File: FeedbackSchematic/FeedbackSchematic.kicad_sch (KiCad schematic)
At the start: 3 parts

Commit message: invert pin read and finish schematic
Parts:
- added C1, C3, C4: 10u, symbol Device:C
- added C2: 47u, symbol Device:C
- added D1, D11, D12, D2, D21, D22, D31, D32, D41, D42, D51, D52, D61, D62, D71, D72: 1N5822, Diode_THT:D_DO-201AD_P15.24mm_Horizontal, symbol Diode:1N5822
- added D100: 1N4001, Diode_THT:D_DO-41_SOD81_P10.16mm_Horizontal, symbol Diode:1N4001
- added J1: Screw_Terminal_01x02, symbol Connector:Screw_Terminal_01x02
- added J10, J11: Conn_01x02_Male, symbol Connector:Conn_01x02_Male
- added J2: Screw_Terminal_01x08, symbol Connector:Screw_Terminal_01x08
- added J3, J4, J5: Conn_01x08_Male, symbol Connector:Conn_01x08_Male
- added J6, J7: RJ45, symbol Connector:RJ45
- added J8: Conn_01x04_Male, symbol Connector:Conn_01x04_Male
- added J9: Conn_01x03_Male, symbol Connector:Conn_01x03_Male
- added R100, R11, R21, R31, R41, R51, R61, R71: 22k, symbol Device:R
- added R101, R104: 330, symbol Device:R
- added R102, R103: 2k2, symbol Device:R
- added R105: 120, symbol Device:R
- added R12, R22, R32, R42, R52, R62, R72: 4.7k, symbol Device:R
- added R13, R23, R3, R33, R43, R53, R63, R73: 22, symbol Device:R
- added U2, U3: L7805, symbol Regulator_Linear:L7805
- added U4, U5: 6N137, Package_DIP:DIP-8_W7.62mm, symbol Isolator:6N137
- added U6: TJA1050_Board, symbol Symbols_Marcel:TJA1050_Board
- gave numbers to parts that had none: 1
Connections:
- net A5: now reaches U1.10 (PA5_SCK1)
- net A5: now also R51.2, R52.1
- net A6: now reaches U1.11 (PA6_MISO1)
- net A6: now also R61.2, R62.1
- net A7: now reaches U1.12 (PA7_MOSI1)
- net A7: now also R71.2, R72.1
- net at U1.19 (GND): now also J10.1 (Pin_1)
- net at U1.20 (GND): now also J10.2 (Pin_2)
- net at U1.21 (PB12): now also J9.1 (Pin_1)
- net at U1.22 (PB13_SCK2): now also J9.2 (Pin_2)
- net at U1.23 (PB14_MISO2): now also J9.3 (Pin_3)
- net at U1.25 (PA8): now also R100.2
- net at U1.26 (PA9_TX1): now also J8.1 (Pin_1)
- net at U1.27 (PA10_RX1): now also J8.2 (Pin_2)
- net CAN_Rx: now reaches U1.28 (PA11_USB_D-)
- net CAN_Rx: now also J8.3 (Pin_3), R102.1, U5.6 (VO)
- net CAN_Tx: now reaches U1.29 (PA12_USBD+)
- net CAN_Tx: now also J8.4 (Pin_4), U4.3 (C)
- net at U1.30 (PA15): now also J3.1 (Pin_1)
- net at U1.31 (PB3): now also J3.2 (Pin_2)
- net at U1.32 (PB4): now also J3.3 (Pin_3)
- net at U1.33 (PB5): now also J3.4 (Pin_4)
- net at U1.34 (PB6_SCL1): now also J3.5 (Pin_5)
- net at U1.35 (PB7_SDA1): now also J3.6 (Pin_6)
- net at U1.36 (PB8): now also J3.7 (Pin_7)
- net at U1.37 (PB9): now also J3.8 (Pin_8)
- net 5V: now reaches U1.38 (5V_USB)
- net 5V: now also R1.1, C2.1, J4.1 (Pin_1), J4.2 (Pin_2), J4.3 (Pin_3), J4.4 (Pin_4), J4.5 (Pin_5), J4.6 (Pin_6), J4.7 (Pin_7), J4.8 (Pin_8), R11.1, R21.1, R31.1, R41.1, R51.1, R61.1, R71.1, U2.3 (OUT), U5.7 (EN), U5.8 (VCC)
- net GND: now reaches U1.39 (GND)
- net GND: now also R2.2, C1.2, C2.2, D1.1 (K), D2.2 (A), J1.1 (Pin_1), J2.8 (Pin_8), J5.1 (Pin_1), J5.2 (Pin_2), J5.3 (Pin_3), J5.4 (Pin_4), J5.5 (Pin_5), J5.6 (Pin_6), J5.7 (Pin_7), J5.8 (Pin_8), R3.1, U2.2 (GND), U5.5 (GND)
- net 3V3: now reaches U1.40 (VCC3V3)
- net 3V3: now also R101.1, R102.2
- net A0: now reaches U1.5 (PA0)
- net A0: now also R1.2, R2.1
- net A1: now reaches U1.6 (PA1)
- net A1: now also R11.2, R12.1
- net A2: now reaches U1.7 (PA2_TX2)
- net A2: now also R21.2, R22.1
- net A3: now reaches U1.8 (PA3_RX2)
- net A3: now also R31.2, R32.1
- net A4: now reaches U1.9 (PA4)
- net A4: now also R41.2, R42.1
- new net: R101.2, U4.2 (A)
- new net: C3.2, C4.1, J6.6, J7.6, U3.2 (GND), U4.5 (GND), U6.1 (GND)
- new net: R103.1, U4.6 (VO), U6.2 (RX)
- new net: C3.1, R103.2, R104.2, U3.3 (OUT), U4.7 (EN), U4.8 (VCC), U6.4 (VCC)
- new net: D1.2 (A), D11.2 (A), D12.1 (K), D2.1 (K), D21.2 (A), D22.1 (K), D31.2 (A), D32.1 (K), D41.2 (A), D42.1 (K), D51.2 (A), D52.1 (K), D61.2 (A), D62.1 (K), D71.2 (A), D72.1 (K), R13.2, R23.2, R3.2, R33.2, R43.2, R53.2, R63.2, R73.2
- new net: C4.2, J6.7, J7.7, U3.1 (IN)
- new net: J6.1, J7.1
- new net: J6.2, J7.2
- new net: J6.3, J7.3
- new net: J11.2 (Pin_2), J6.4, J7.4, R105.1, U6.5 (CAN_L), U6.6 (CAN_H)
- new net: J6.5, J7.5
- new net: J6.8, J7.8
- new net: U5.3 (C), U6.3 (TX)
- new net: R104.1, U5.2 (A)
- new net: J11.1 (Pin_1), R105.2
- new net: C1.1, D100.1 (K), U2.1 (IN)
- new net Dcc1: D100.2 (A), J1.2 (Pin_2), R100.1
- new net Track1: D11.1 (K), D12.2 (A), J2.7 (Pin_7), R12.2, R13.1
- new net Track2: D21.1 (K), D22.2 (A), J2.6 (Pin_6), R22.2, R23.1
- new net Track3: D31.1 (K), D32.2 (A), J2.5 (Pin_5), R32.2, R33.1
- new net Track4: D41.1 (K), D42.2 (A), J2.4 (Pin_4), R42.2, R43.1
- new net Track5: D51.1 (K), D52.2 (A), J2.3 (Pin_3), R52.2, R53.1
- new net Track6: D61.1 (K), D62.2 (A), J2.2 (Pin_2), R62.2, R63.1
- new net Track7: D71.1 (K), D72.2 (A), J2.1 (Pin_1), R72.2, R73.1
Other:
- moved on the sheet: R1, R2, U1

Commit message: Updated schematics
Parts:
- added D110, D111, D112, D113, D114, D115, D116, D117, D120, D121, D122, D123, D124, D125, D126, D127: LED, symbol Device:LED
- added R110, R111, R112, R113, R114, R115, R116, R117, R120, R121, R122, R123, R124, R125, R126, R127: 470, symbol Device:R
- added U6, U7: 74HC595, symbol 74xx:74HC595
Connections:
- net 5V: now also U6.16 (VCC), U7.16 (VCC)
- net GND: now also D110.1 (K), D111.1 (K), D112.1 (K), D113.1 (K), D114.1 (K), D115.1 (K), D116.1 (K), D117.1 (K), D120.1 (K), D121.1 (K), D122.1 (K), D123.1 (K), D124.1 (K), D125.1 (K), D126.1 (K), D127.1 (K), U6.13 (~{OE}), U6.8 (GND), U7.13 (~{OE}), U7.8 (GND)
- net LedClk: now reaches U1.13 (PB0)
- net LedClk: now also U6.11 (SRCLK), U7.11 (SRCLK)
- net LedData: now reaches U1.14 (PB1)
- net LedData: now also U6.14 (SER)
- net LedOut: now reaches U1.15 (PB10_SCL2)
- net LedOut: now also U6.12 (RCLK), U7.12 (RCLK)
- net LedReset: now reaches U1.16 (PB11_SDA2)
- net LedReset: now also U6.10 (~{SRCLR}), U7.10 (~{SRCLR})
- new net: R113.1, U6.3 (QD)
- new net: D113.2 (A), R113.2
- new net: R111.1, U6.1 (QB)
- new net: R110.1, U6.15 (QA)
- new net: R112.1, U6.2 (QC)
- new net: R114.1, U6.4 (QE)
- new net: R115.1, U6.5 (QF)
- new net: R116.1, U6.6 (QG)
- new net: R117.1, U6.7 (QH)
- new net: U6.9 (QH'), U7.14 (SER)
- new net: R123.1, U7.3 (QD)
- new net: D123.2 (A), R123.2
- new net: R121.1, U7.1 (QB)
- new net: R120.1, U7.15 (QA)
- new net: R122.1, U7.2 (QC)
- new net: R124.1, U7.4 (QE)
- new net: R125.1, U7.5 (QF)
- new net: R126.1, U7.6 (QG)
- new net: R127.1, U7.7 (QH)
- new net: D110.2 (A), R110.2
- new net: D126.2 (A), R126.2
- new net: D116.2 (A), R116.2
- new net: D114.2 (A), R114.2
- new net: D112.2 (A), R112.2
- new net: D120.2 (A), R120.2
- new net: D124.2 (A), R124.2
- new net: D111.2 (A), R111.2
- new net: D122.2 (A), R122.2
- new net: D125.2 (A), R125.2
- new net: D117.2 (A), R117.2
- new net: D121.2 (A), R121.2
- new net: D127.2 (A), R127.2
- new net: D115.2 (A), R115.2
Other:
- moved on the sheet: J10, J3, J4, J5, J8, J9, R100, U1

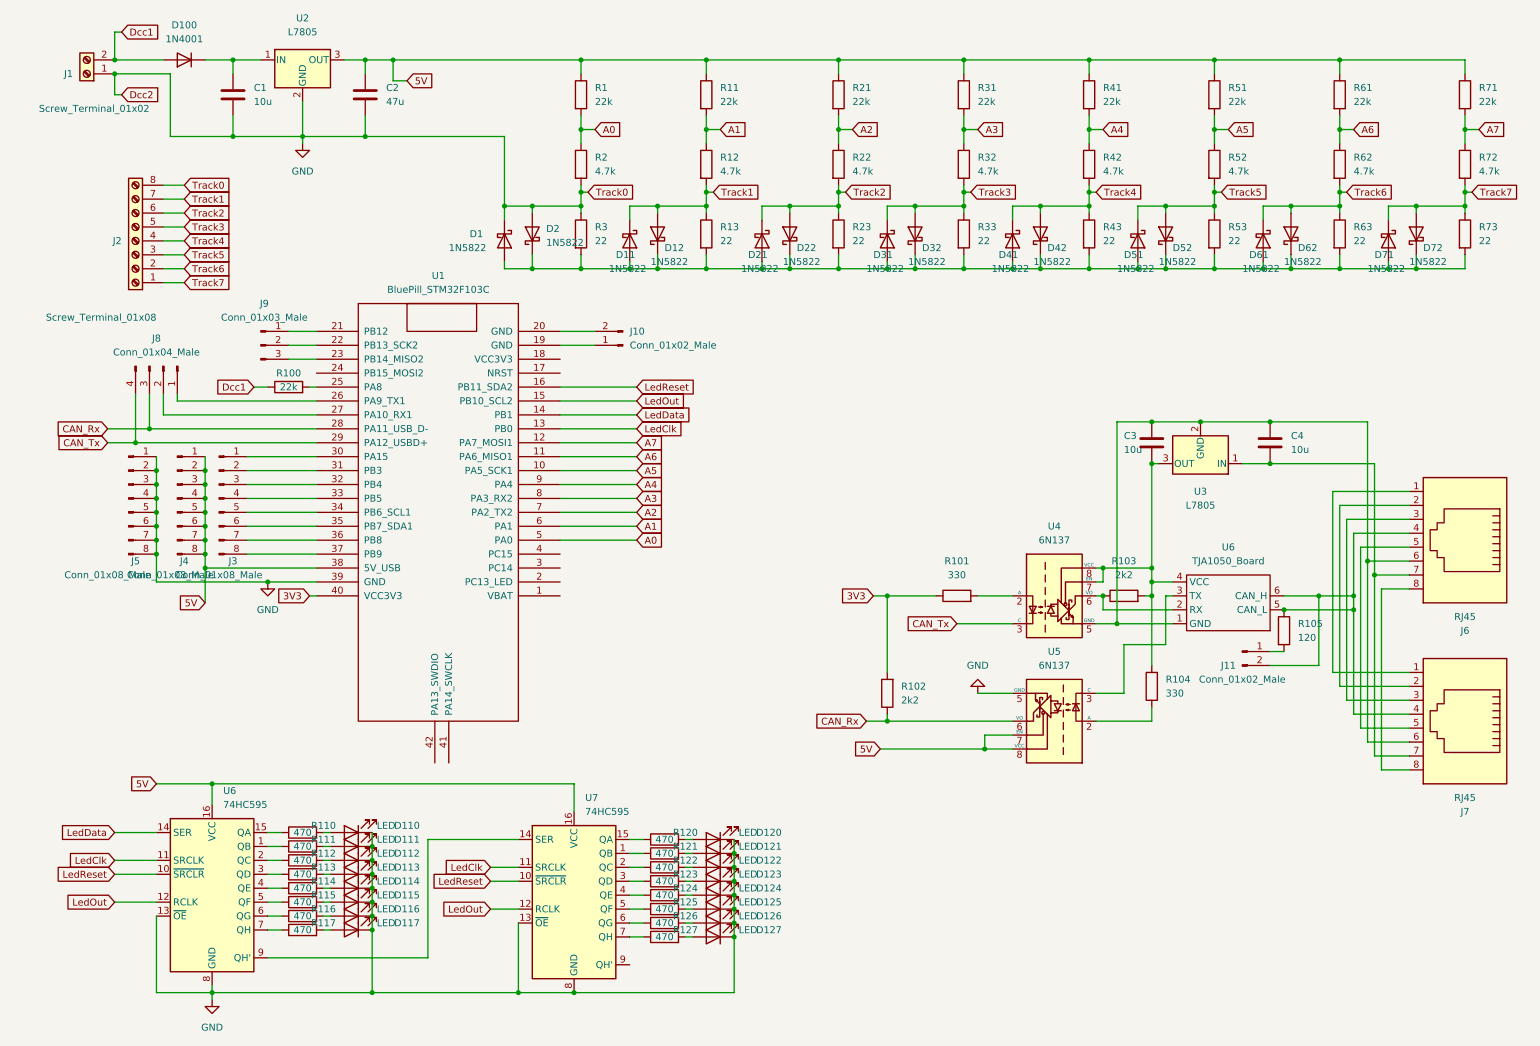
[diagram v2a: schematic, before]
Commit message: Added footprints except tja1050
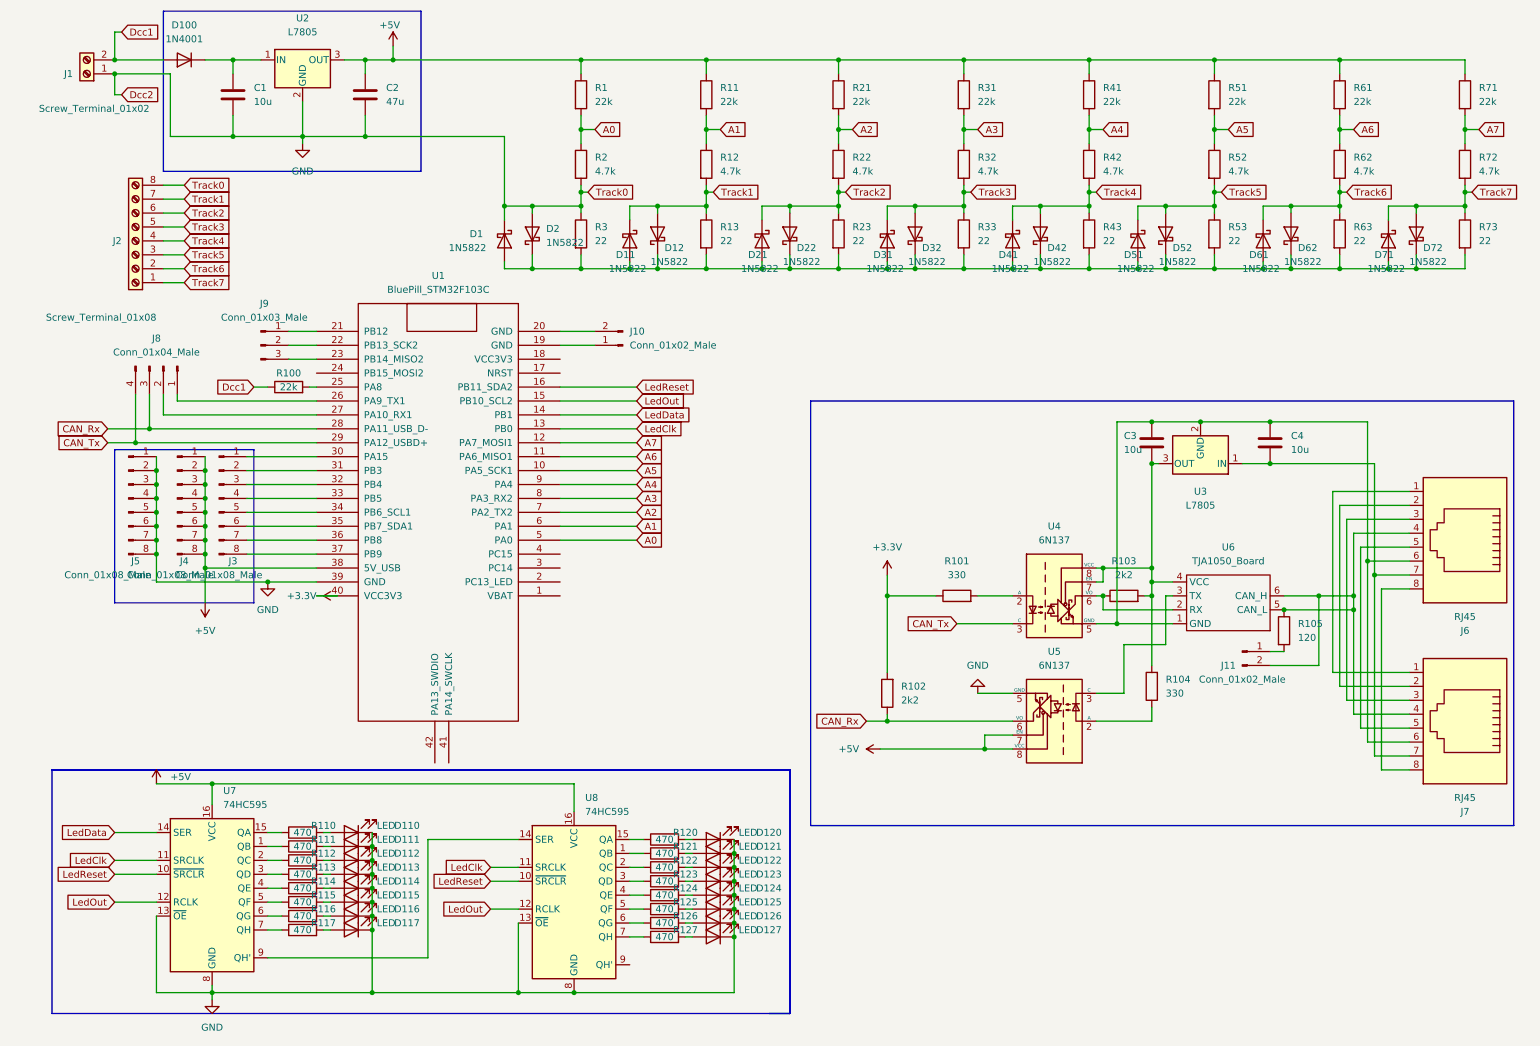
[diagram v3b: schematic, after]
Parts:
- C1, C2, C3, C4: footprint (none) -> Capacitor_THT:CP_Radial_D5.0mm_P2.00mm
- D110, D111, D112, D113, D114, D115, D116, D117, D120, D121, D122, D123, D124, D125, D126, D127: footprint (none) -> LED_THT:LED_D3.0mm_Horizontal_O1.27mm_Z2.0mm
- J1: footprint (none) -> TerminalBlock_RND:TerminalBlock_RND_205-00002_1x03_P5.00mm_Horizontal
- J10, J11: footprint (none) -> Connector_PinHeader_2.54mm:PinHeader_1x02_P2.54mm_Vertical
- J2: footprint (none) -> TerminalBlock_RND:TerminalBlock_RND_205-00018_1x08_P5.00mm_Horizontal
- J3, J4, J5: footprint (none) -> Connector_PinHeader_2.54mm:PinHeader_1x08_P2.54mm_Vertical
- J6, J7: footprint (none) -> Connector_RJ:RJ45_Amphenol_54602-x08_Horizontal
- J8: footprint (none) -> Connector_PinHeader_2.54mm:PinHeader_1x04_P2.54mm_Vertical
- J9: footprint (none) -> Connector_PinHeader_2.54mm:PinHeader_1x03_P2.54mm_Vertical
- R1, R100, R101, R102, R103, R104, R105, R11, R110, R111, R112, R113, R114, R115, R116, R117, R12, R120, R121, R122, R123, R124, R125, R126, R127, R2, R21, R22, R3, R31, R32, R41, R42, R51, R52, R61, R62, R71, R72: footprint (none) -> Resistor_THT:R_Axial_DIN0204_L3.6mm_D1.6mm_P5.08mm_Horizontal
- R13, R23, R33, R43, R53, R63, R73: footprint (none) -> Resistor_THT:R_Axial_DIN0204_L3.6mm_D1.6mm_P1.90mm_Vertical
- U2, U3: footprint (none) -> Package_TO_SOT_THT:TO-220-3_Vertical
- U7: renamed from U6; footprint (none) -> Package_DIP:DIP-14_W7.62mm_Socket
- U8: renamed from U7; footprint (none) -> Package_DIP:DIP-14_W7.62mm_Socket
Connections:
- net 3V3 renamed +3.3V
- net 5V renamed +5V
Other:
- title: (none) -> Feedback CAN Decoder

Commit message: Updated footprint
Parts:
- J1: footprint TerminalBlock_RND:TerminalBlock_RND_205-00002_1x03_P5.00mm_Horizontal -> TerminalBlock_RND:TerminalBlock_RND_205-00012_1x02_P5.00mm_Horizontal
- U1: footprint BluePill_breakouts:BluePill_STM32F103C -> Footprint_Marcel:Bluepill
- U6: footprint (none) -> Footprint_Marcel:TJA1050
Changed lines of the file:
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@@
     (stroke (width 0) (type default) (color 0 0 0 0))
   )
-  (wire (pts (xy 68.58 120.65) (xy 64.77 120.65))
-    (stroke (width 0) (type default) (color 0 0 0 0))
-  )
   (wire (pts (xy 55.88 186.69) (xy 85.09 186.69))
     (stroke (width 0) (type default) (color 0 0 0 0))
@@
     (property "Reference" "U1" (id 0) (at 86.995 62.23 0))
     (property "Value" "BluePill_STM32F103C" (id 1) (at 86.995 64.77 0))
-    (property "Footprint" "BluePill_breakouts:BluePill_STM32F103C" (id 2) (at 86.36 62.23 0)
+    (property "Footprint" "Footprint_Marcel:Bluepill" (id 2) (at 86.36 62.23 0)
       (effects (font (size 1.27 1.27)) hide)
     )
@@
     (property "Reference" "U6" (id 0) (at 231.14 111.76 0))
     (property "Value" "TJA1050_Board" (id 1) (at 231.14 114.3 0))
-    (property "Footprint" "" (id 2) (at 231.14 115.57 0)
+    (property "Footprint" "Footprint_Marcel:TJA1050" (id 2) (at 231.14 115.57 0)
       (effects (font (size 1.27 1.27)) hide)
     )
@@
       (effects (font (size 1.27 1.27)) (justify left))
     )
-    (property "Footprint" "TerminalBlock_RND:TerminalBlock_RND_205-00002_1x03_P5.00mm_Horizontal" (id 2) (at 22.86 25.4 0)
+    (property "Footprint" "TerminalBlock_RND:TerminalBlock_RND_205-00012_1x02_P5.00mm_Horizontal" (id 2) (at 22.86 25.4 0)
       (effects (font (size 1.27 1.27)) hide)
     )
@@
     (pin "2")
   )
-  (symbol (lib_id "power:+3.3V") (at 68.58 120.65 90) (unit 1)
-    (in_bom yes) (on_board yes) (fields_autoplaced)
-    (property "Reference" "#PWR04" (id 0) (at 72.39 120.65 0)
+  (symbol (lib_id "power:+3.3V") (at 64.77 120.65 90) (unit 1)
+    (in_bom yes) (on_board yes)
+    (property "Reference" "#PWR04" (id 0) (at 68.58 120.65 0)
       (effects (font (size 1.27 1.27)) hide)
     )
-    (property "Value" "+3.3V" (id 1) (at 64.77 120.6499 90)
+    (property "Value" "+3.3V" (id 1) (at 64.77 123.19 90)
       (effects (font (size 1.27 1.27)) (justify left))
     )
-    (property "Footprint" "" (id 2) (at 68.58 120.65 0)
+    (property "Footprint" "" (id 2) (at 64.77 120.65 0)
       (effects (font (size 1.27 1.27)) hide)
     )
-    (property "Datasheet" "" (id 3) (at 68.58 120.65 0)
+    (property "Datasheet" "" (id 3) (at 64.77 120.65 0)
       (effects (font (size 1.27 1.27)) hide)
     )
@@
     )
     (path "/8cf2a6b6-ba53-4401-8b5b-6d344d0b7e0e"
-      (reference "J1") (unit 1) (value "Screw_Terminal_01x02") (footprint "TerminalBlock_RND:TerminalBlock_RND_205-00002_1x03_P5.00mm_Horizontal")
+      (reference "J1") (unit 1) (value "Screw_Terminal_01x02") (footprint "TerminalBlock_RND:TerminalBlock_RND_205-00012_1x02_P5.00mm_Horizontal")
     )
     (path "/f68b0618-192e-4836-84f5-d0253d207d5a"
@@
     )
     (path "/1065cb5f-54ca-45cc-b2ab-e8803f30a939"
-      (reference "U1") (unit 1) (value "BluePill_STM32F103C") (footprint "BluePill_breakouts:BluePill_STM32F103C")
+      (reference "U1") (unit 1) (value "BluePill_STM32F103C") (footprint "Footprint_Marcel:Bluepill")
     )
     (path "/e604f0f9-1111-4069-a4eb-9c5688696bf6"
@@
     )
     (path "/63950369-1610-449f-b07e-5ef80631f63c"
-      (reference "U6") (unit 1) (value "TJA1050_Board") (footprint "")
+      (reference "U6") (unit 1) (value "TJA1050_Board") (footprint "Footprint_Marcel:TJA1050")
     )
     (path "/1ab9b1bd-eda3-477d-a65e-83d660ed9f83"
